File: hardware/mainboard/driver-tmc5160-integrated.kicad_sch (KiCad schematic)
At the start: 33 parts, among them M6 Micro-Fit 3.0, Q10 DMT6016LFDF, Q11 DMT6016LFDF, Q4 DMT6016LFDF, Q5 DMT6016LFDF, Q6 DMT6016LFDF, Q7 DMT6016LFDF, Q8 DMT6016LFDF, Q9 DMT6016LFDF, U1 TMC5160A-TA

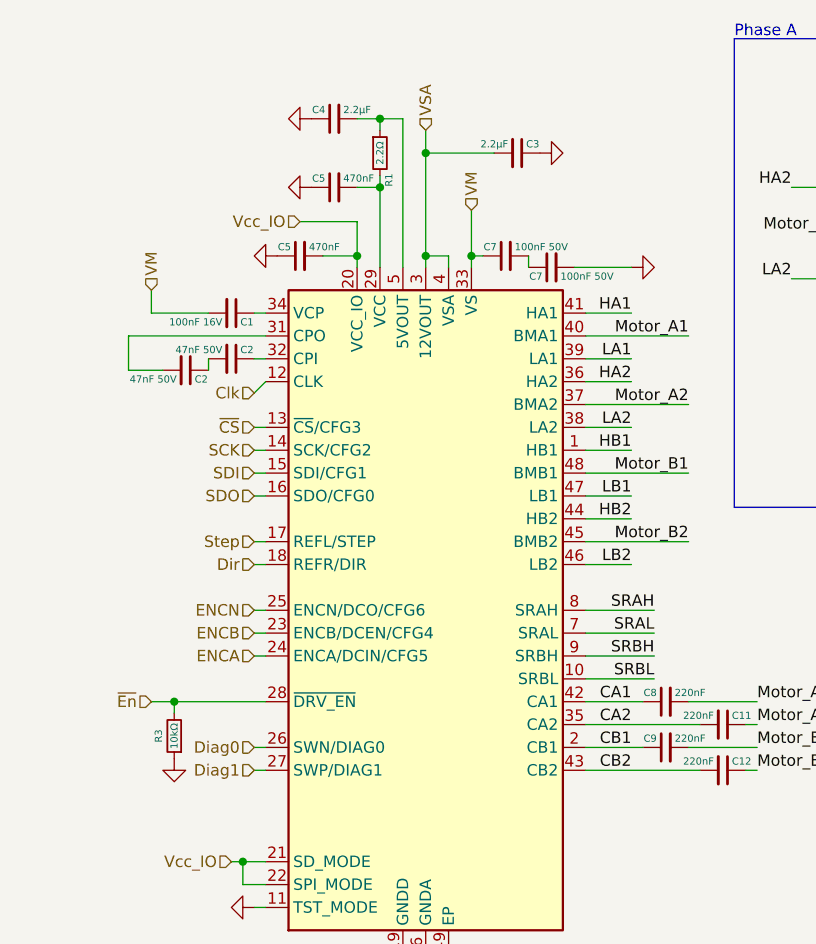
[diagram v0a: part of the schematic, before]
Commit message: tested SMD style XH connectors — didn't work very well alas
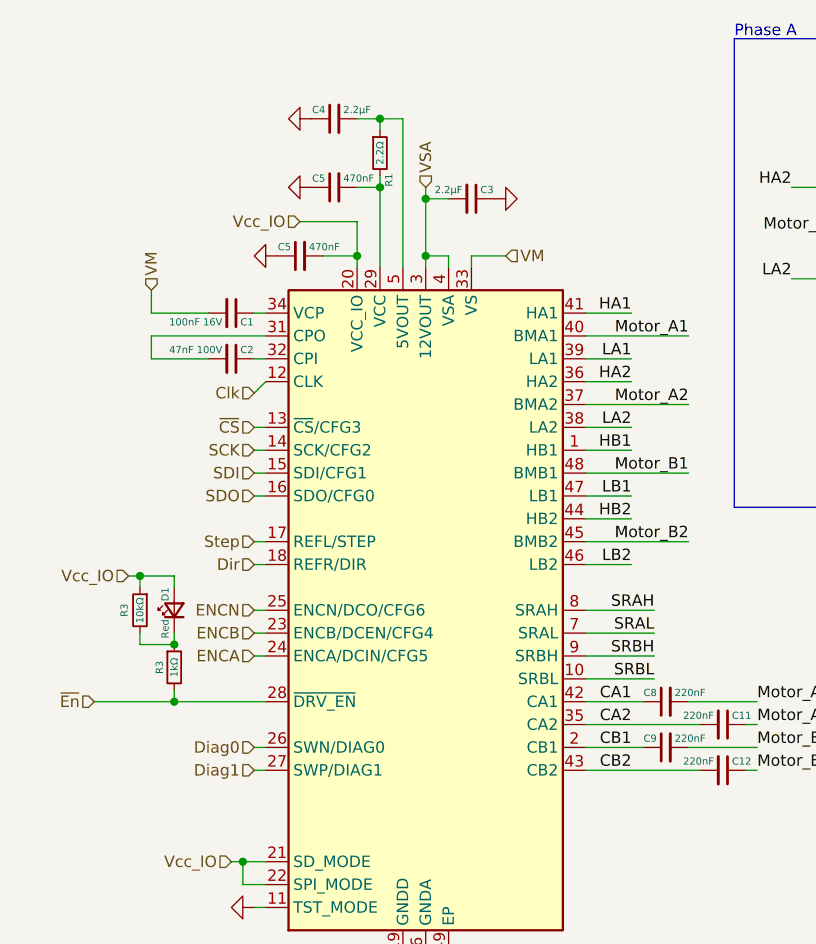
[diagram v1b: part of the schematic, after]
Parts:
- removed C2: 47nF 50V, AlphaLib:0402C, symbol Device:C_Small
- removed C7 (x2): 100nF 50V, AlphaLib:0402C, symbol Device:C_Small
- added D1: Red, AlphaLib:0402LED, symbol Device:LED_Small
- added R3: 1kΩ, AlphaLib:0402R, symbol Device:R_Small
- C2: value 47nF 50V -> 47nF 100V
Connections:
- net GND: no longer R3.1
- net Vcc_IO: now also R3.1, D1.2 (A)
- net ~{En}: now also R3.2; no longer R3.2
- net at C2.2: now also U1.31 (CPO)
- new net: D1.1 (K), R3.1, R3.2
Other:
- moved on the sheet: C3, R3

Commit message: fan ports
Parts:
- removed R3: 10kΩ, AlphaLib:0402R, symbol Device:R_Small
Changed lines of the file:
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@@
   (junction (at 27.94 88.9) (diameter 0) (color 0 0 0 0)
   )
-  (junction (at 27.94 82.55) (diameter 0) (color 0 0 0 0)
-  )
-  (junction (at 24.13 74.93) (diameter 0) (color 0 0 0 0)
-  )
   (junction (at 53.34 119.38) (diameter 0) (color 0 0 0 0)
   )
@@
     (stroke (width 0) (type default))
   )
-  (wire (pts (xy 24.13 82.55) (xy 27.94 82.55))
-    (stroke (width 0) (type default))
-  )
-  (wire (pts (xy 24.13 81.28) (xy 24.13 82.55))
-    (stroke (width 0) (type default))
-  )
   (wire (pts (xy 149.86 31.75) (xy 153.67 31.75))
     (stroke (width 0) (type default))
@@
     (stroke (width 0) (type default))
   )
-  (wire (pts (xy 24.13 74.93) (xy 24.13 76.2))
-    (stroke (width 0) (type default))
-  )
   (wire (pts (xy 36.83 96.52) (xy 38.1 96.52))
     (stroke (width 0) (type default))
   )
-  (wire (pts (xy 22.86 74.93) (xy 24.13 74.93))
+  (wire (pts (xy 22.86 74.93) (xy 27.94 74.93))
     (stroke (width 0) (type default))
   )
@@
   )
   (wire (pts (xy 104.14 57.15) (xy 109.22 57.15))
-    (stroke (width 0) (type default))
-  )
-  (wire (pts (xy 24.13 74.93) (xy 27.94 74.93))
     (stroke (width 0) (type default))
   )
@@
         )
       )
-    )
-  )
-  (symbol (lib_id "Device:R_Small") (at 24.13 78.74 0) (mirror y) (unit 1)
-    (in_bom yes) (on_board yes) (dnp no)
-    (property "Reference" "R3" (at 22.86 78.74 90)
-      (effects (font (size 0.8 0.8)) (justify top))
-    )
-    (property "Value" "10kΩ" (at 24.13 78.74 90)
-      (effects (font (size 0.8 0.8)))
-    )
-    (property "Footprint" "AlphaLib:0402R" (at 24.13 78.74 0)
-      (effects (font (size 1.27 1.27)) hide)
-    )
-    (property "Datasheet" "~" (at 24.13 78.74 0)
-      (effects (font (size 1.27 1.27)) hide)
-    )
-    (pin "1")
-    (pin "2")
-    (instances
-      (project "driver-tmc5160"
-        (path "/03364e55-5655-494a-997e-0cd456c2d9b5"
-          (reference "R3") (unit 1)
-        )
-      )
-      (project "mainboard"
-        (path "/1a565782-f217-442e-b118-196625f31c53"
-          (reference "R104") (unit 1)
-        )
-        (path "/1a565782-f217-442e-b118-196625f31c53/972ca71f-1c40-4278-8cb4-2b520c3e8975"
-          (reference "R98") (unit 1)
-        )
-        (path "/1a565782-f217-442e-b118-196625f31c53/99778979-7977-44ff-ba7b-f489010f8682"
-          (reference "R114") (unit 1)
-        )
-        (path "/1a565782-f217-442e-b118-196625f31c53/f6e6a5bb-7803-4b0b-883d-433919711a15"
-          (reference "R115") (unit 1)
-        )
-        (path "/1a565782-f217-442e-b118-196625f31c53/64a332d7-9292-493c-af4b-24f0e80d7999"
-          (reference "R116") (unit 1)
-        )
-        (path "/1a565782-f217-442e-b118-196625f31c53/09bb4a8f-8694-4b82-8e1f-fabe3bd11ec7"
-          (reference "R31") (unit 1)
-        )
-        (path "/1a565782-f217-442e-b118-196625f31c53/d34aeff3-da22-4edc-92e0-1591d6117dbc"
-          (reference "R39") (unit 1)
-        )
-      )

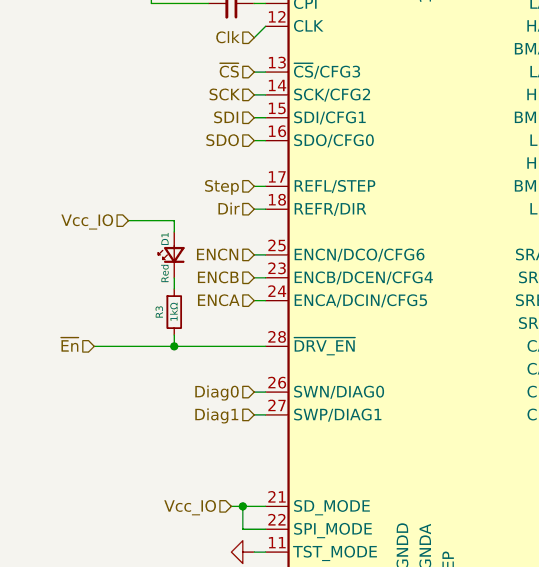
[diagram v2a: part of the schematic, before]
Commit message: this is immediately before i switch the terminus USB hub with the corechips
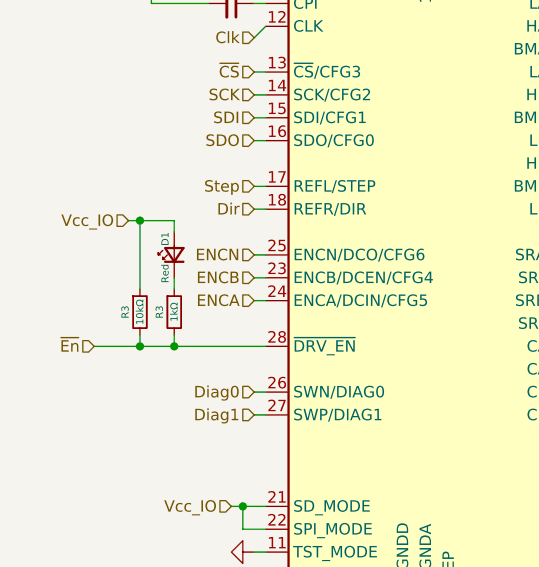
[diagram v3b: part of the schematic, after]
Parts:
- added R3: 10kΩ, AlphaLib:0402R, symbol Device:R_Small
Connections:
- net Vcc_IO: now also R3.1
- net ~{En}: now also R3.2
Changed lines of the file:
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@@
     (comment 1 "High voltage, high current stepper motor driver block powered by the TMC2160/5160 chip")
   )
+  (junction (at 24.13 88.9) (diameter 0) (color 0 0 0 0)
+  )
   (junction (at 158.75 36.83) (diameter 0) (color 0 0 0 0)
   )
@@
   (junction (at 130.81 36.83) (diameter 0) (color 0 0 0 0)
   )
+  (junction (at 24.13 74.93) (diameter 0) (color 0 0 0 0)
+  )
   (junction (at 118.11 46.99) (diameter 0) (color 0 0 0 0)
   )
@@
     (stroke (width 0) (type default))
   )
+  (wire (pts (xy 24.13 74.93) (xy 27.94 74.93))
+    (stroke (width 0) (type default))
+  )
   (wire (pts (xy 85.09 55.88) (xy 73.66 55.88))
     (stroke (width 0) (type default))
@@
     (stroke (width 0) (type default))
   )
+  (wire (pts (xy 24.13 88.9) (xy 27.94 88.9))
+    (stroke (width 0) (type default))
+  )
   (wire (pts (xy 154.94 91.44) (xy 166.37 91.44))
     (stroke (width 0) (type default))
@@
     (stroke (width 0) (type default))
   )
-  (wire (pts (xy 19.05 88.9) (xy 27.94 88.9))
+  (wire (pts (xy 19.05 88.9) (xy 24.13 88.9))
     (stroke (width 0) (type default))
   )
@@
     (stroke (width 0) (type default))
   )
+  (wire (pts (xy 24.13 74.93) (xy 24.13 82.55))
+    (stroke (width 0) (type default))
+  )
   (wire (pts (xy 116.84 52.07) (xy 118.11 52.07))
     (stroke (width 0) (type default))
@@
     (stroke (width 0) (type default))
   )
-  (wire (pts (xy 22.86 74.93) (xy 27.94 74.93))
+  (wire (pts (xy 22.86 74.93) (xy 24.13 74.93))
     (stroke (width 0) (type default))
   )
@@
   )
   (wire (pts (xy 160.02 21.59) (xy 163.83 21.59))
+    (stroke (width 0) (type default))
+  )
+  (wire (pts (xy 24.13 87.63) (xy 24.13 88.9))
     (stroke (width 0) (type default))
   )
@@
         )
       )
+    )
+  )
+  (symbol (lib_id "Device:R_Small") (at 24.13 85.09 0) (unit 1)
+    (in_bom yes) (on_board yes) (dnp no)
+    (property "Reference" "R3" (at 22.5 85.09 90)
+      (effects (font (size 0.8 0.8)))
+    )
+    (property "Value" "10kΩ" (at 24.13 85.09 90)
+      (effects (font (size 0.8 0.8)))
+    )
+    (property "Footprint" "AlphaLib:0402R" (at 24.13 85.09 0)
+      (effects (font (size 1.27 1.27)) hide)
+    )
+    (property "Datasheet" "~" (at 24.13 85.09 0)
+      (effects (font (size 1.27 1.27)) hide)
+    )
+    (pin "1")
+    (pin "2")
+    (instances
+      (project "driver-tmc5160"
+        (path "/03364e55-5655-494a-997e-0cd456c2d9b5"
+          (reference "R3") (unit 1)
+        )
+      )
+      (project "mainboard"
+        (path "/1a565782-f217-442e-b118-196625f31c53"
+          (reference "R96") (unit 1)
+        )
+        (path "/1a565782-f217-442e-b118-196625f31c53/956ffa88-460c-45ff-bb37-d040d3cbedfe"
+          (reference "R70") (unit 1)
+        )
+        (path "/1a565782-f217-442e-b118-196625f31c53/28340924-2d90-4a87-bb0b-10ef0633a541"
+          (reference "R71") (unit 1)
+        )
+        (path "/1a565782-f217-442e-b118-196625f31c53/f514cf63-1394-4014-821a-69b4627909f9"
+          (reference "R72") (unit 1)
+        )
+        (path "/1a565782-f217-442e-b118-196625f31c53/6adaba86-2614-4e1b-b3d6-74260a2c85fe"
+          (reference "R67") (unit 1)
+        )
+        (path "/1a565782-f217-442e-b118-196625f31c53/09bb4a8f-8694-4b82-8e1f-fabe3bd11ec7"
+          (reference "R106") (unit 1)
+        )
+        (path "/1a565782-f217-442e-b118-196625f31c53/d34aeff3-da22-4edc-92e0-1591d6117dbc"
+          (reference "R107") (unit 1)
+        )
+      )

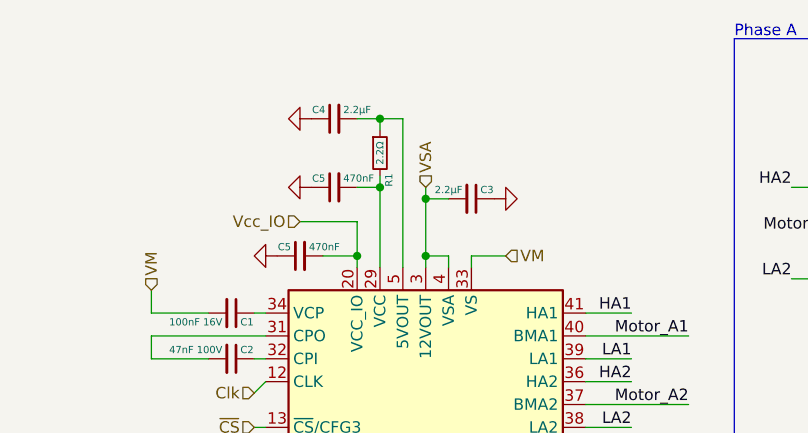
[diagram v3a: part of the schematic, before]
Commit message: added more 3D models and created first few renders
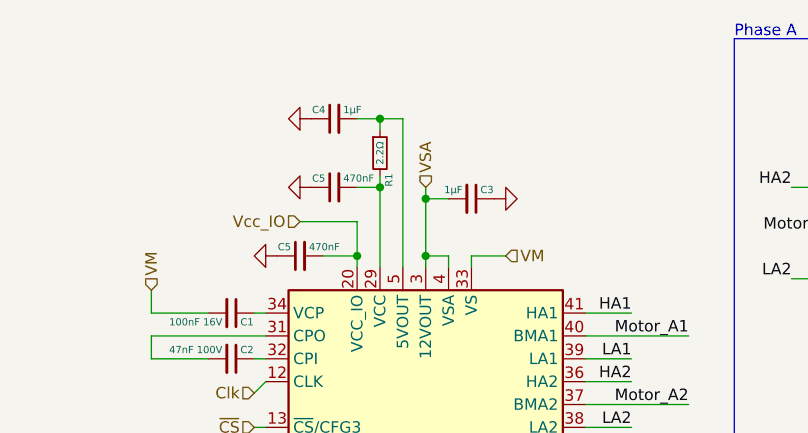
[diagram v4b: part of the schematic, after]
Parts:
- C3, C4: value 2.2μF -> 1μF
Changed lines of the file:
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@@
       (effects (font (size 0.8 0.8)) (justify left))
     )
-    (property "Value" "2.2μF" (at 46.72 23.13 90)
+    (property "Value" "1μF" (at 46.72 23.13 90)
       (effects (font (size 0.8 0.8)) (justify right))
     )
@@
       (effects (font (size 0.8 0.8)) (justify left))
     )
-    (property "Value" "2.2μF" (at 59.96 32.02 90)
-      (effects (font (size 0.8 0.8)) (justify right))
-    )
+    (property "Value" "1μF" (at 59.96 32.02 90)
+      (effects (font (size 0.8 0.8)) (justify right))
+    )
